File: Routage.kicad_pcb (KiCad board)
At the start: 2 copper layers, 110 x 100 mm, 56 parts, among them J2 Conn_01x02, J3 Conn_01x03, Q1 2N2907, Q10 TIP32, Q11 BD138, Q12 TIP31, Q13 2N2222, Q2 2N2907, Q3 2N2907, Q4 2N2222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

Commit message: Version 2 du placement + DRC
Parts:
- moved C7 103.9 mm to (34.3, 47.0), turned to 0 degrees
- moved R16 86.7 mm to (25.4, 66.0), turned to 0 degrees
- moved C4 80.0 mm to (40.6, 30.5)
- moved Q8 76.5 mm to (113.0, 64.8), turned to 180 degrees
- moved R9 71.3 mm to (124.5, 110.5), turned to 90 degrees
- moved HS2 70.0 mm to (110.5, 69.8)
- moved Q10 68.7 mm to (108.0, 74.9)
- moved C6 68.6 mm to (45.7, 41.9)
- moved R6 67.4 mm to (43.2, 85.1)
- moved C2 66.2 mm to (27.9, 102.9), turned to 270 degrees
- moved RV2 62.7 mm to (105.4, 110.5)
- moved R11 61.9 mm to (100.3, 39.4), turned to 180 degrees
- moved Q6 60.5 mm to (100.3, 101.6), turned to 180 degrees
- moved C8 59.5 mm to (86.4, 68.6), turned to 180 degrees
- moved R15 58.0 mm to (66.0, 69.8), turned to 180 degrees
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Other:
- net class Default: clearance 0.2 -> 0.3; trace_width 0.25 -> 0.6; via_dia 0.8 -> 2.1; via_drill 0.4 -> 0.6
- rule trace_clearance: 0.2 -> 0.3
- rule trace_min: 0.2 -> 0.4
- rule via_min_drill: 0.3 -> 0.6
- rule via_min_size: 0.4 -> 0.6

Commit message: Placement_V2 après validation et correction des derniers détails
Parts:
- moved Q12 4.02 mm to (113.0, 48.3), turned to 180 degrees
- moved Q8 2.54 mm to (113.0, 67.3)
- moved HS1 1.27 mm to (110.5, 52.1)
- moved Q10 1.27 mm to (108.0, 73.7)

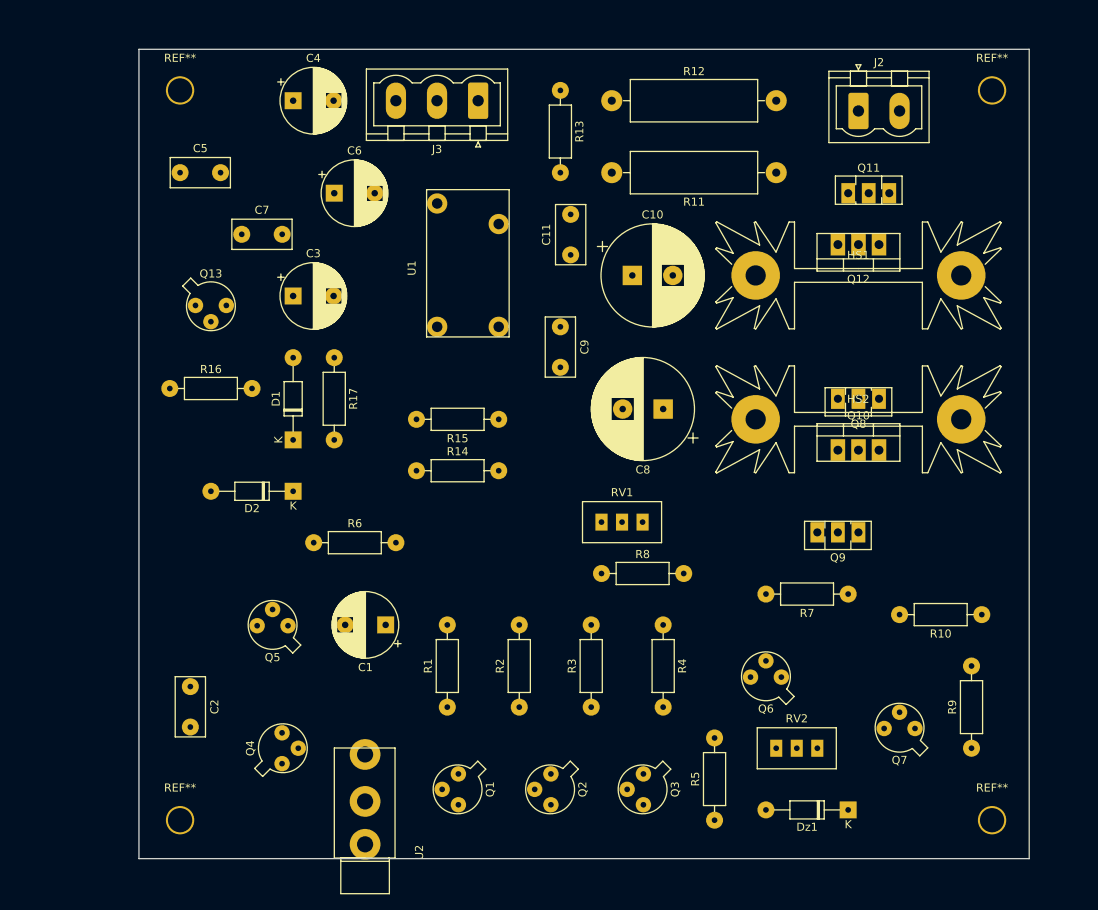
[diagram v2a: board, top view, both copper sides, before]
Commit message: V1 du routage + Changement placement + rajout diode + Pb masse
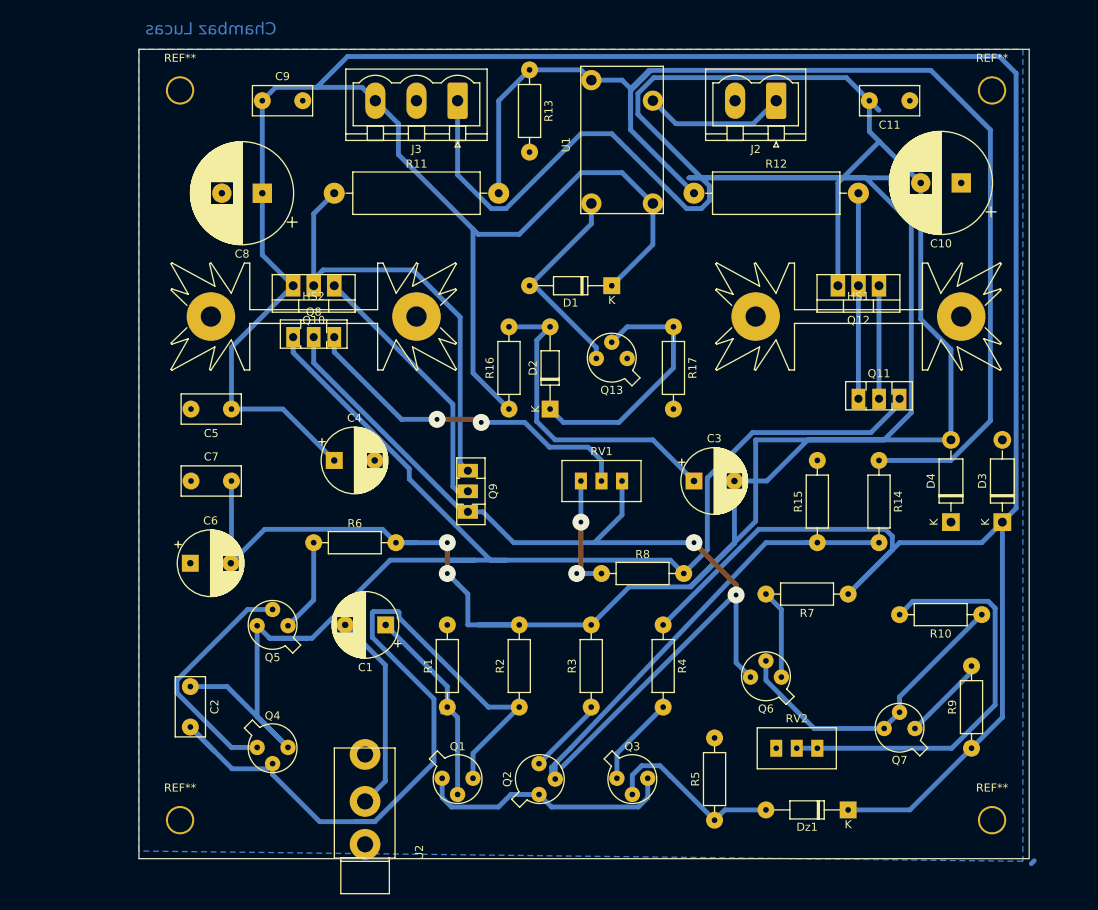
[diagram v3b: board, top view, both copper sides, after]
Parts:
- added D3: 1N4001, Diode_THT:D_DO-41_SOD81_P10.16mm_Horizontal, F.Cu at (128.3, 82.5)
- added D4: 1N4001, Diode_THT:D_DO-41_SOD81_P10.16mm_Horizontal, F.Cu at (121.9, 82.5)
- moved Q8 72.8 mm to (40.6, 59.7), turned to 0 degrees
- moved HS2 68.5 mm to (43.2, 57.1)
- moved Q10 65.5 mm to (45.7, 53.3), turned to 180 degrees
- moved R14 57.2 mm to (113.0, 74.9), turned to 270 degrees
- moved C8 56.3 mm to (36.8, 41.9)
- moved R11 54.7 mm to (45.7, 41.9), turned to 0 degrees
- moved C3 54.6 mm to (90.2, 77.5)
- moved Q13 52.5 mm to (81.3, 62.2), turned to 180 degrees
- moved C6 49.1 mm to (27.9, 87.6)
- moved Q9 48.9 mm to (62.2, 76.2), turned to 270 degrees
- moved C9 46.2 mm to (36.8, 30.5), turned to 0 degrees
- moved C11 46.0 mm to (116.8, 30.5), turned to 180 degrees
- moved C4 44.7 mm to (45.7, 74.9)
- moved D1 43.7 mm to (80.0, 53.3), turned to 180 degrees
- moved C10 42.2 mm to (123.2, 40.6), turned to 180 degrees
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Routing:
- net -12V: track 0.00 -> 420.4 mm, vias 0 -> 2
- net +12V: track 0.00 -> 416.6 mm
- net Net-(C2-Pad1): track 0.00 -> 178.3 mm
- net Net-(R11-Pad2): track 0.00 -> 156.7 mm
- net Net-(Q6-Pad3): track 0.00 -> 118.1 mm, vias 0 -> 2
- net Net-(C2-Pad2): track 0.00 -> 102.2 mm
- net Net-(Q2-Pad2): track 0.00 -> 55.9 mm
- net Net-(Q10-Pad2): track 0.00 -> 53.6 mm
- net Net-(R10-Pad2): track 0.00 -> 51.5 mm
- net Net-(Q8-Pad3): track 0.00 -> 43.6 mm, vias 0 -> 2
- net Net-(C3-Pad1): track 0.00 -> 39.9 mm
- net Net-(Q6-Pad2): track 0.00 -> 38.5 mm
- net Net-(Q10-Pad1): track 0.00 -> 33.0 mm
- net Net-(Q1-Pad1): track 0.00 -> 32.4 mm
- net Net-(D2-Pad1): track 0.00 -> 32.2 mm
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- added copper zone on B.Cu, net GND
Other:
- board text added: "Chambaz Lucas"

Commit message: V2 Routage après avoir refait le placement
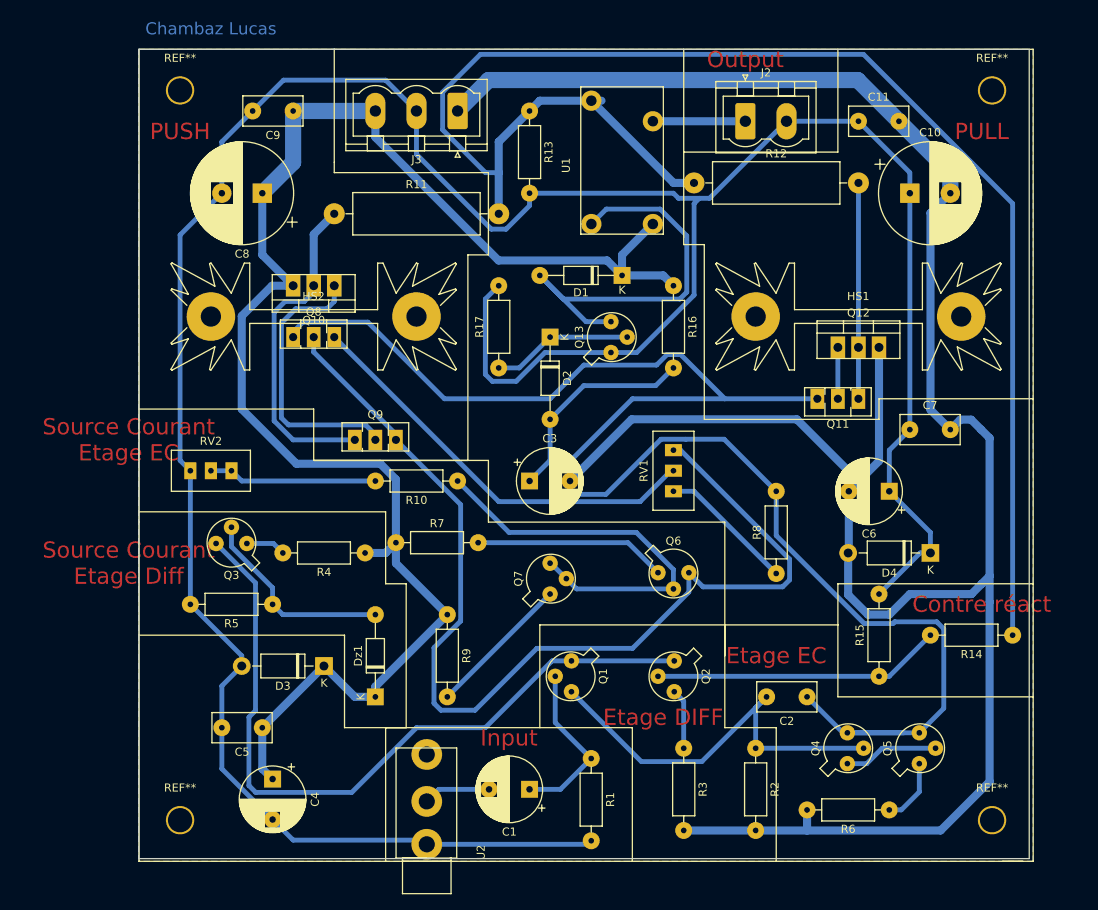
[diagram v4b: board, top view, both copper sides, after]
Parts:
- moved C7 89.0 mm to (116.8, 71.1)
- moved C6 86.8 mm to (114.3, 78.7), turned to 180 degrees
- moved D3 85.7 mm to (44.5, 100.3), turned to 180 degrees
- moved Q5 80.5 mm to (118.1, 111.8), turned to 90 degrees
- moved RV2 80.1 mm to (33.0, 76.2)
- moved R6 78.4 mm to (114.3, 118.1), turned to 180 degrees
- moved C2 76.2 mm to (104.1, 104.1), turned to 180 degrees
- moved Q4 72.4 mm to (109.2, 111.8), turned to 90 degrees
- moved R10 66.8 mm to (61.0, 77.5)
- moved R9 66.8 mm to (59.7, 94.0), turned to 270 degrees
- moved R5 60.8 mm to (38.1, 92.7), turned to 180 degrees
- moved Dz1 60.1 mm to (50.8, 104.1), turned to 90 degrees
- moved R7 56.2 mm to (53.3, 85.1), turned to 0 degrees
- moved Q3 55.3 mm to (34.3, 85.1), turned to 180 degrees
- moved Q7 47.5 mm to (72.5, 90.8), turned to 90 degrees
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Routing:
- net GND: track 0.00 -> 355.0 mm
- net +12V: track 416.6 -> 195.7 mm
- net -12V: track 420.4 -> 289.2 mm, vias 2 -> 0
- net Net-(Q1-Pad1): track 32.4 -> 91.9 mm
- net Net-(C2-Pad2): track 102.2 -> 51.2 mm
- net Net-(R11-Pad2): track 156.7 -> 187.7 mm
- net Net-(R10-Pad2): track 51.5 -> 20.8 mm
- net Net-(D1-Pad2): track 26.1 -> 51.8 mm
- net Net-(C2-Pad1): track 178.3 -> 201.5 mm
- net Net-(Q2-Pad2): track 55.9 -> 35.8 mm
- net Net-(Q4-Pad1): track 29.7 -> 11.7 mm
- net Net-(C1-Pad2): track 24.9 -> 8.32 mm
- net Net-(D2-Pad1): track 32.2 -> 17.5 mm
- net Net-(C3-Pad1): track 39.9 -> 26.5 mm
- net Net-(Q6-Pad3): track 118.1 -> 131.1 mm, vias 2 -> 0
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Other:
- board text added: "Contre réact"
- board text added: "Etage DIFF"
- board text added: "Etage EC"
- board text added: "Input"
- board text added: "Output"
- board text added: "PULL"
- board text added: "PUSH"
- board text added: "Source Courant Etage Diff"
- board text added: "Source Courant Etage EC"

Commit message: Version finale avec les derniers défauts corrigés
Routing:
- net GND: track 355.0 -> 373.8 mm
- net Net-(C2-Pad1): track 201.5 -> 215.0 mm
- net Net-(Q6-Pad3): track 131.1 -> 136.6 mm
- net Net-(C2-Pad2): track 51.2 -> 55.7 mm
- net Net-(R11-Pad2): track 187.7 -> 191.3 mm
- net Net-(D1-Pad2): track 51.8 -> 55.3 mm
- net Net-(Q1-Pad1): track 91.9 -> 95.0 mm
- net +12V: track 195.7 -> 197.3 mm
- net Net-(Q10-Pad2): track 41.0 -> 42.5 mm
- net Net-(Q6-Pad2): track 50.2 -> 51.4 mm
- net Net-(Q8-Pad3): track 51.9 -> 53.0 mm
- net -12V: track 289.2 -> 288.4 mm
- net Net-(Q10-Pad1): track 34.4 -> 33.8 mm
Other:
- board text added: "Alim Etage Diff"
- board text added: "Alim Etage EC"
- board text added: "Chambaz - Hérisson"
- board text added: "FeedBack"
- board text removed: "Chambaz Lucas"
- board text removed: "Contre réact"
- board text removed: "Source Courant Etage Diff"
- board text removed: "Source Courant Etage EC"
